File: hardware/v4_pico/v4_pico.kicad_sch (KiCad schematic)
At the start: 92 parts, among them J1 joystick, J2 LED strip, J3 SSD1306 SPI, J4 MIDI OUT Y:M5 - R:M4, J5 Batt, J6 Neck - Y:O BK:B R:3.3, J7 Conn_01x03_Female, J8 MXP5010, Q1 2N7000, U1 74HC165, U2 74HC165, U3 74HC165, U4 Teensy3.2_breadboard_friendly

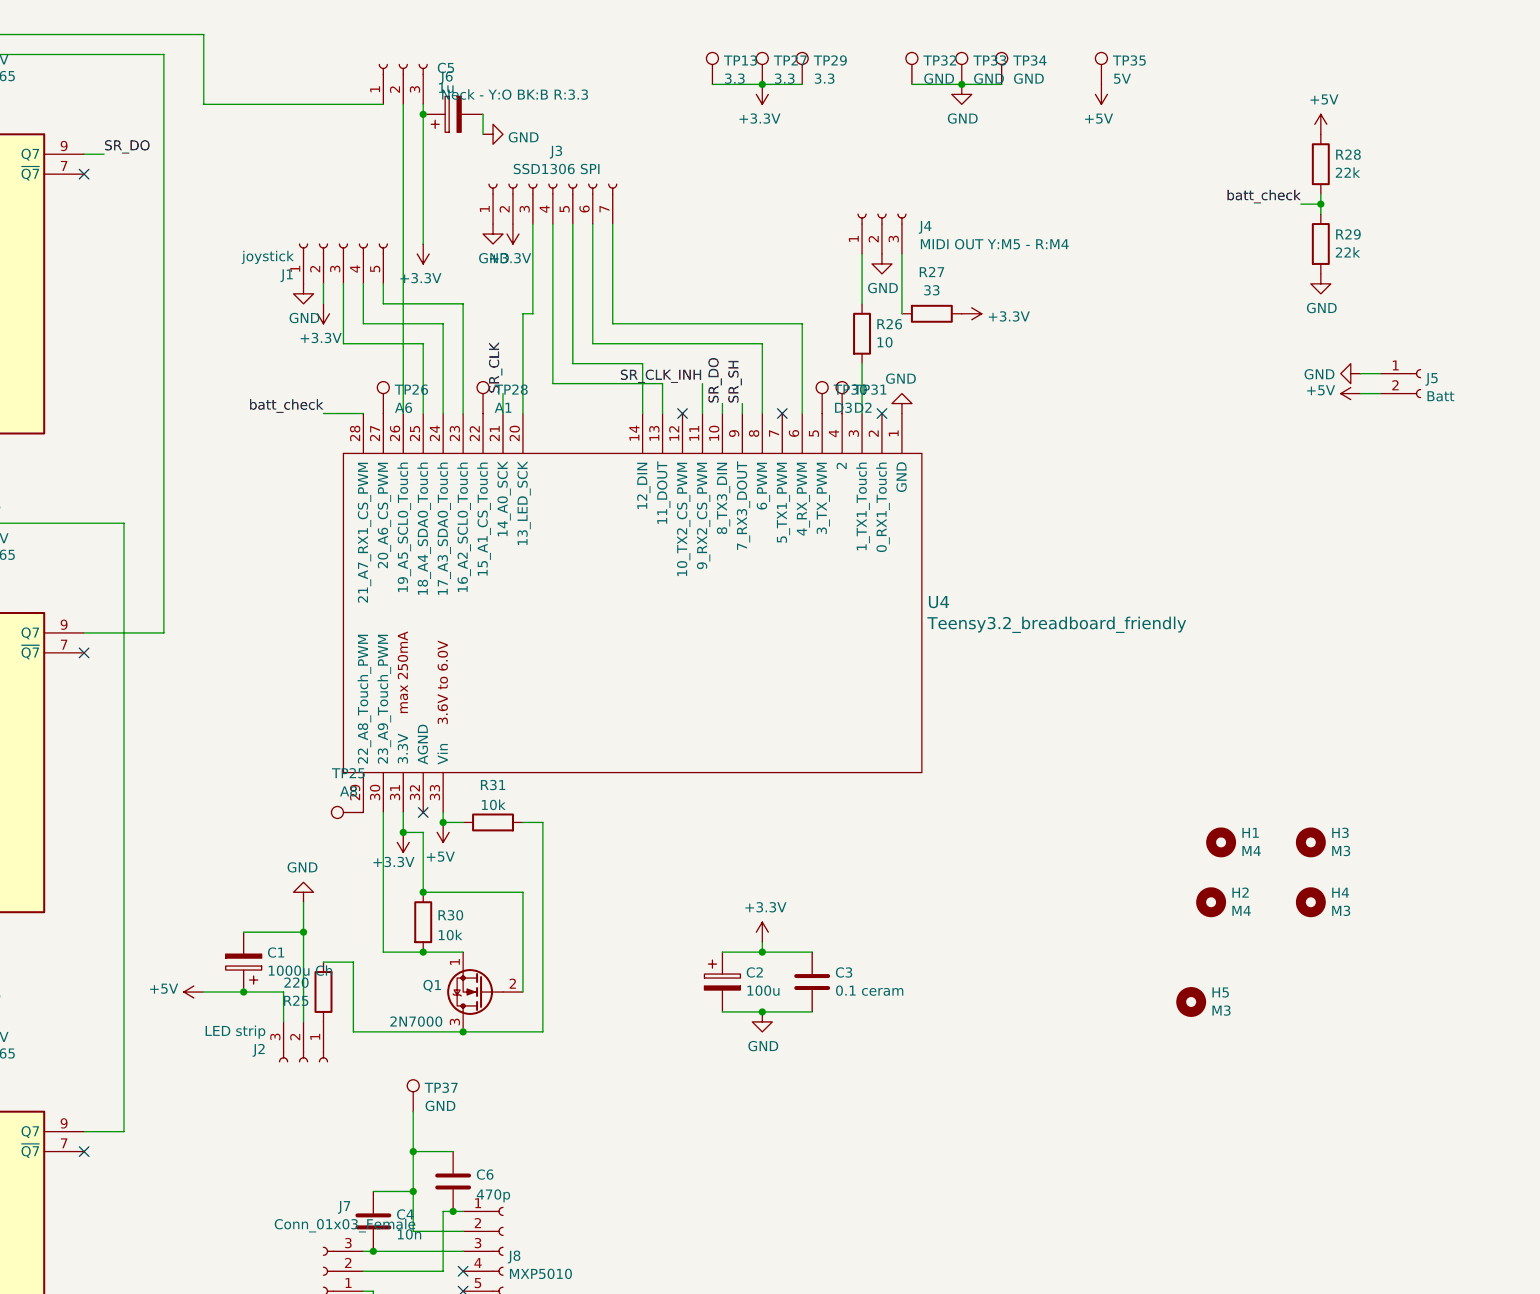
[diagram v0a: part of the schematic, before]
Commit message: Started porting to pico, LED strip and Joystick moved
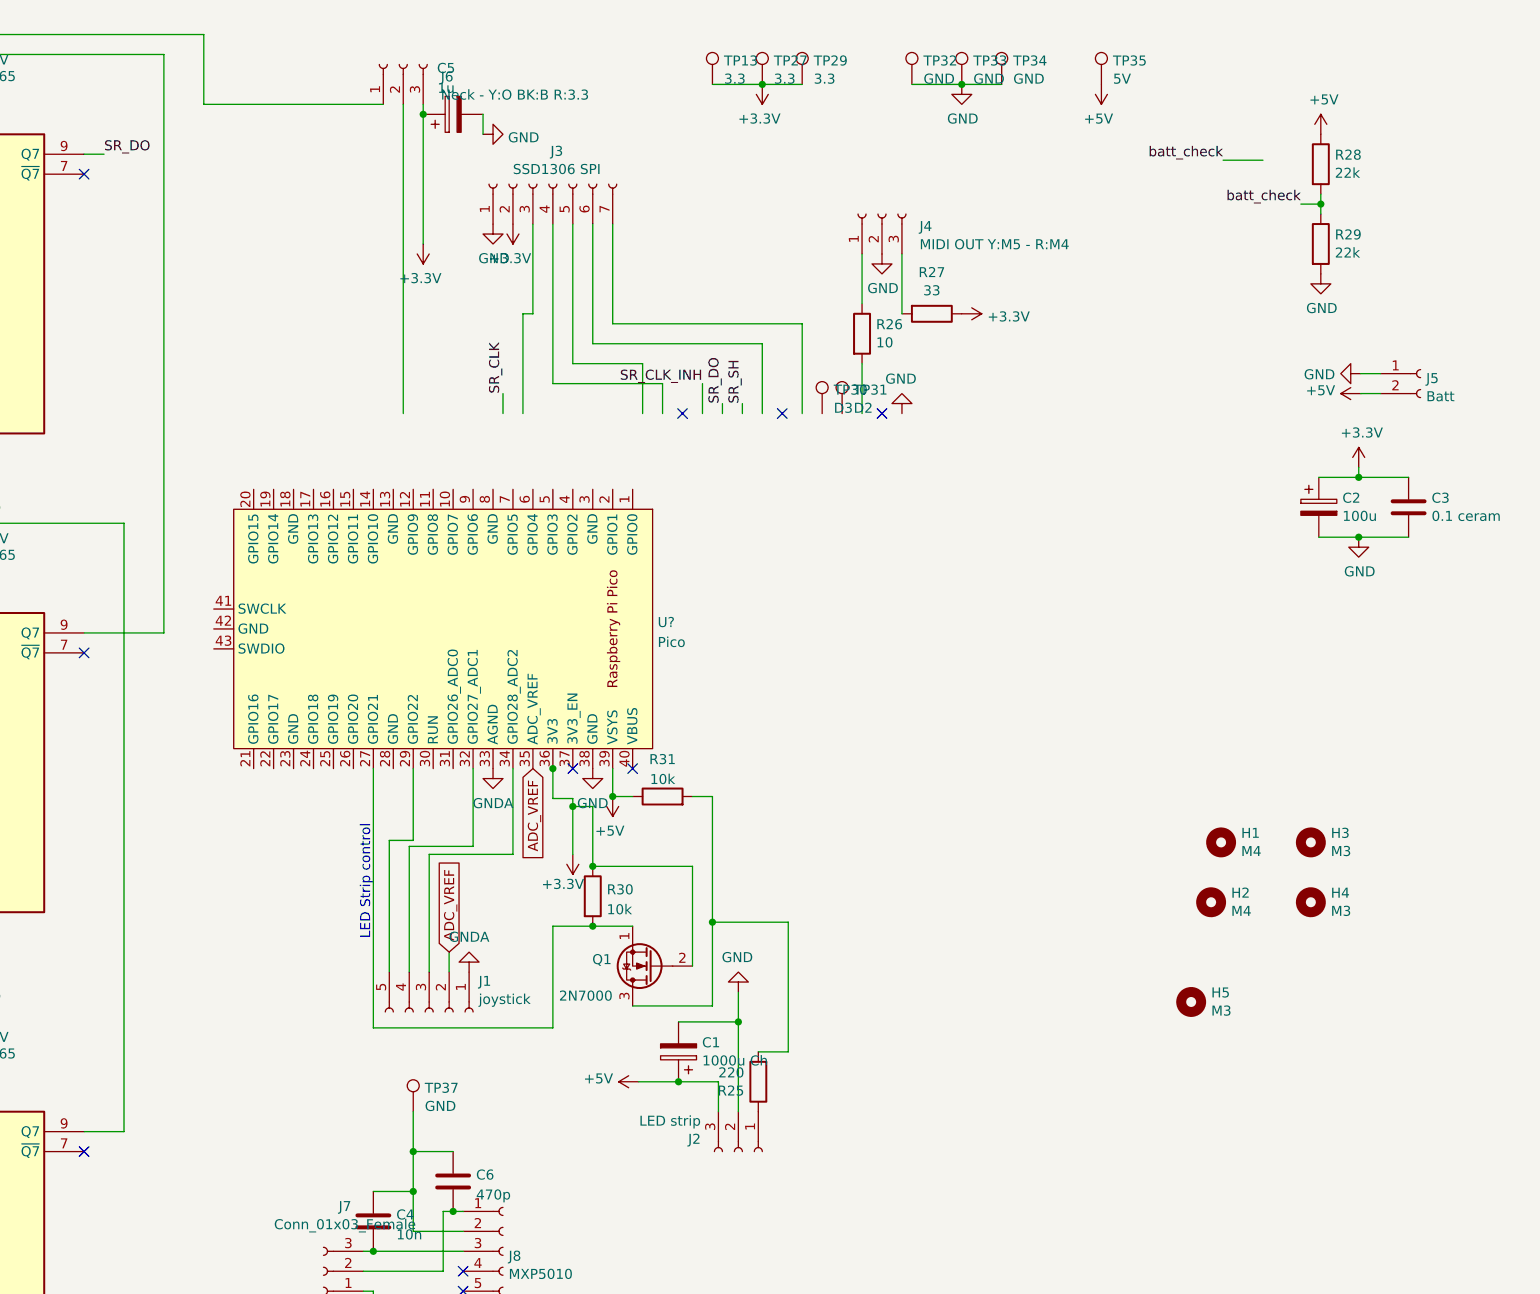
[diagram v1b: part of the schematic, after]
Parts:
- removed TP25: A8, TestPoint:TestPoint_THTPad_2.5x2.5mm_Drill1.2mm, symbol Connector:TestPoint
- removed TP26: A6, TestPoint:TestPoint_THTPad_2.5x2.5mm_Drill1.2mm, symbol Connector:TestPoint
- removed TP28: A1, TestPoint:TestPoint_THTPad_2.5x2.5mm_Drill1.2mm, symbol Connector:TestPoint
- removed U4: Teensy3.2_breadboard_friendly, teensy:Teensy30_31_32_breadboard_friendly_hand_soldering, symbol teensy:Teensy3.2_breadboard_friendly
- added U?: Pico, RPi_Pico:RPi_Pico_SMD_TH, symbol MCU_RaspberryPi_and_Boards:Pico
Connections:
- net +3V3: now also U?.36 (3V3); no longer J1.2 (Pin_2)
- net +5V: now also U?.39 (VSYS)
- net GND: now also U?.38 (GND); no longer J1.1 (Pin_1)
- net at J1.5 (Pin_5): now also U?.29 (GPIO22)
- net at J1.4 (Pin_4): now also U?.32 (GPIO27_ADC1)
- net at J1.3 (Pin_3): now also U?.34 (GPIO28_ADC2)
- net at Q1.1 (S), R30.2: now also U?.27 (GPIO21)
- new net ADC_VREF: J1.2 (Pin_2), U?.35 (ADC_VREF)
- new net GNDA: J1.1 (Pin_1), U?.33 (AGND)
- no-connect marks 12 -> 13
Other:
- note added: "LED Strip control"
- moved on the sheet: C1, C2, C3, J1, J2, Q1, R25, R30, R31

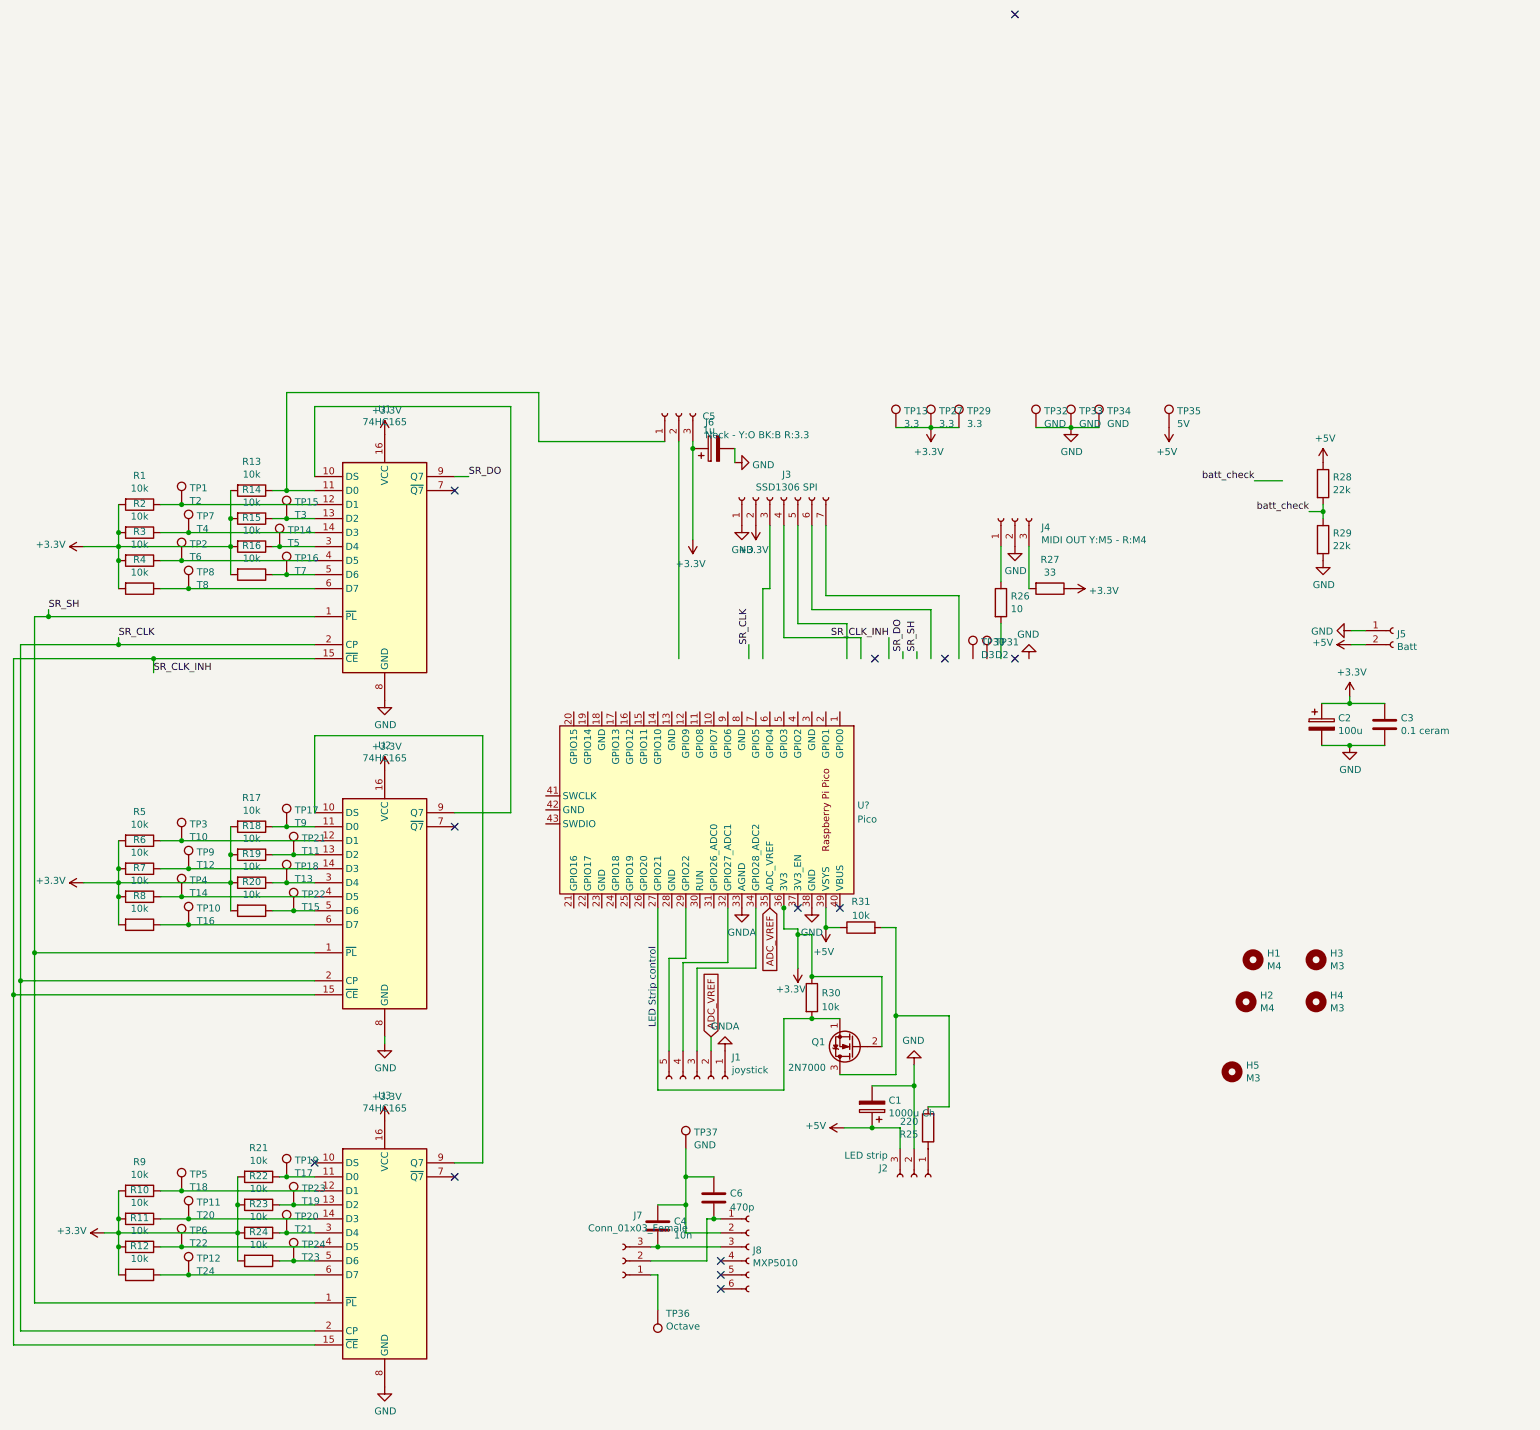
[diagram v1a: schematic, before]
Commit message: Added switch on PCB for on/off, neck updated
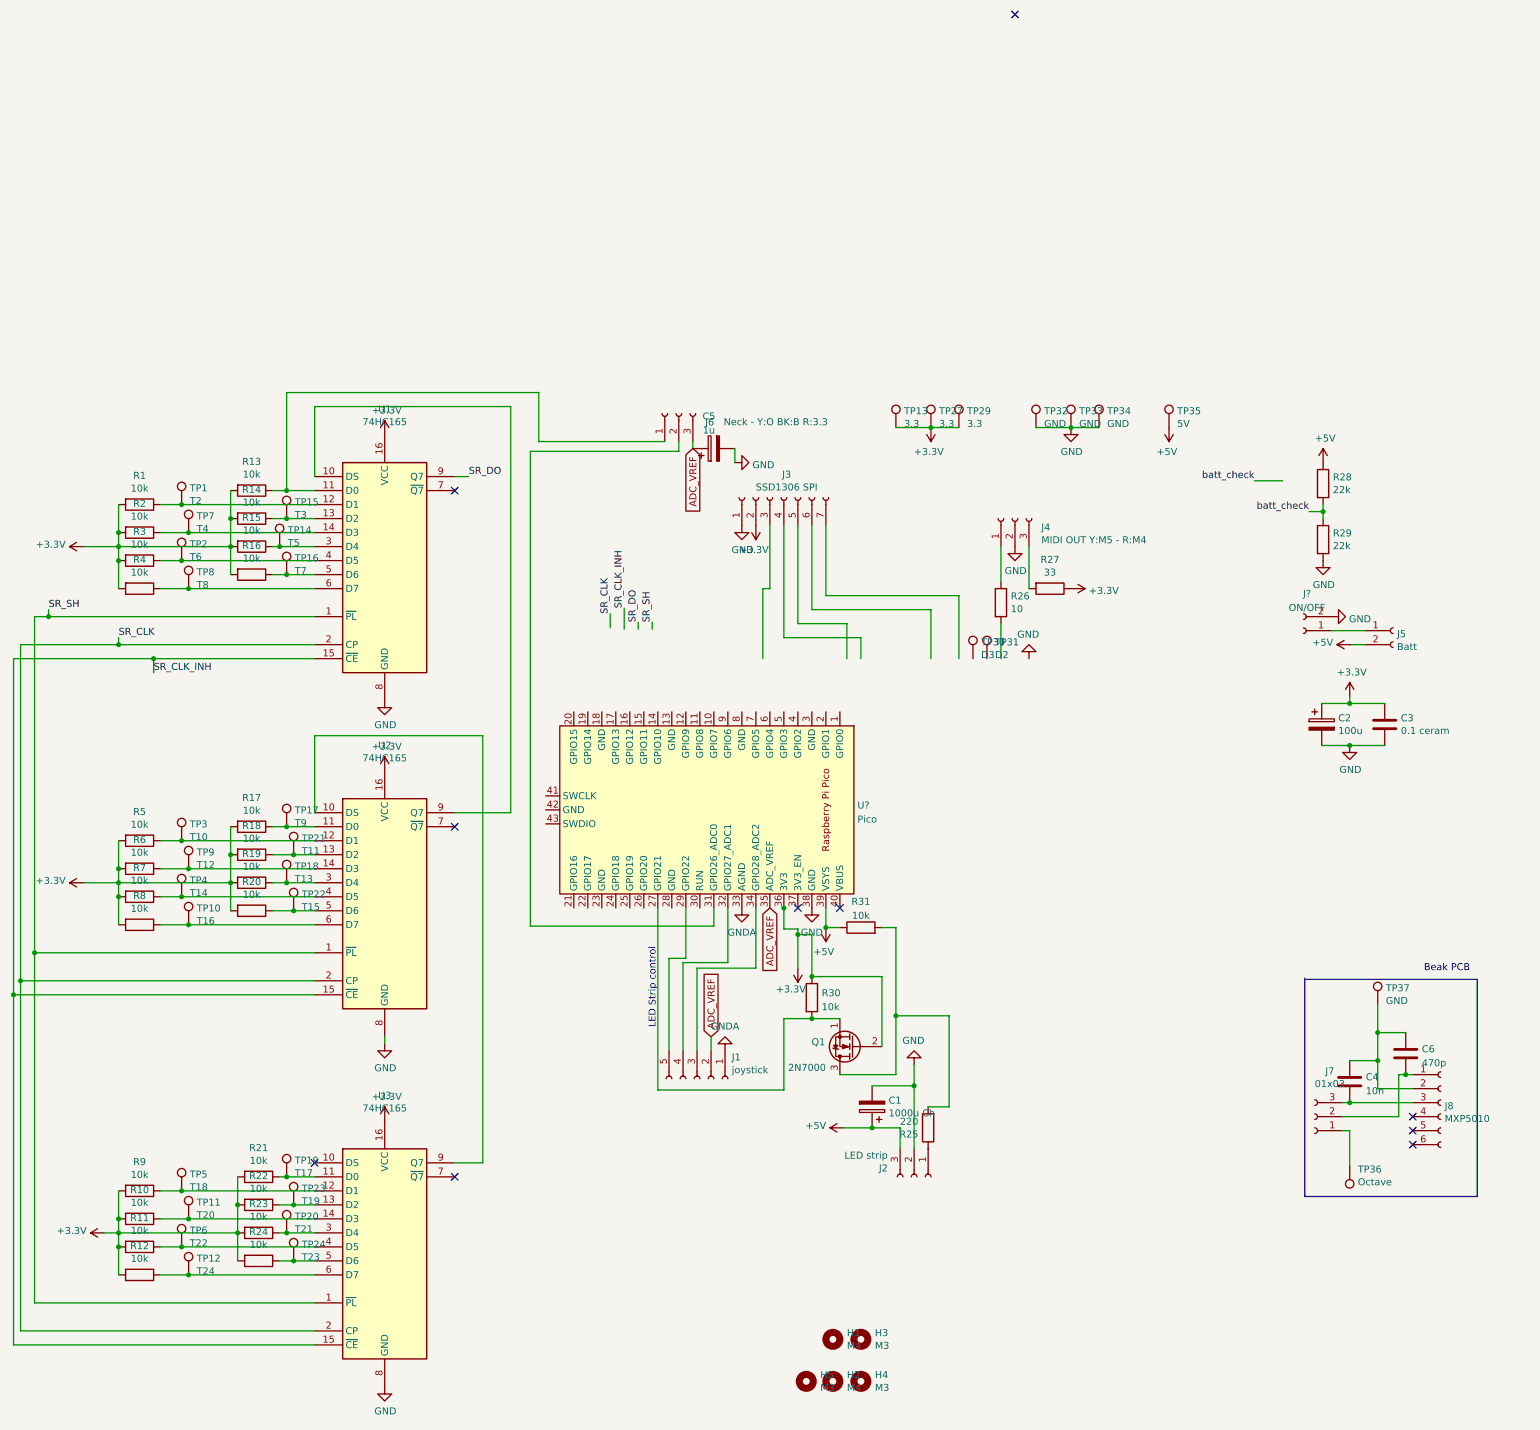
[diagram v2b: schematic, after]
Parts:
- added J?: ON/OFF, symbol Connector:Conn_01x02_Female
- J7: value Conn_01x03_Female -> 01x03
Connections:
- net +3V3: no longer C5.1, J6.3 (Pin_3)
- net ADC_VREF: now also C5.1, J6.3 (Pin_3)
- net GND: now also J?.2 (Pin_2); no longer J5.1 (Pin_1)
- net at J6.2 (Pin_2): now also U?.31 (GPIO26_ADC0)
- new net: J5.1 (Pin_1), J?.1 (Pin_1)
- no-connect marks 13 -> 10
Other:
- note added: "Beak PCB"
- moved on the sheet: C4, C6, H1, H2, H3, H4, H5, J7, J8, TP36, TP37
